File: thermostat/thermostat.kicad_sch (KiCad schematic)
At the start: 14 parts, among them J1 Conn_01x16, J2 Conn_01x12, J3 Conn_01x05, SW1 EVP-AEBB2A, U1 ATSAMD21G18A-A, U2 SPX3819M5-L-3-3, U3 SS-52400-002, Y1 Crystal

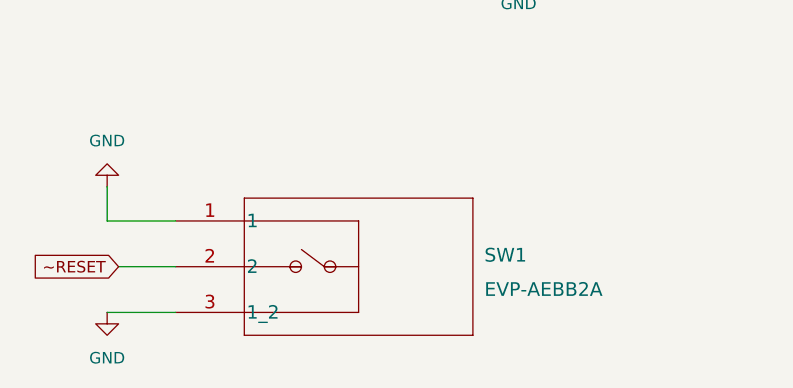
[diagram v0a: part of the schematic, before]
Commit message: thermostat: Use switch
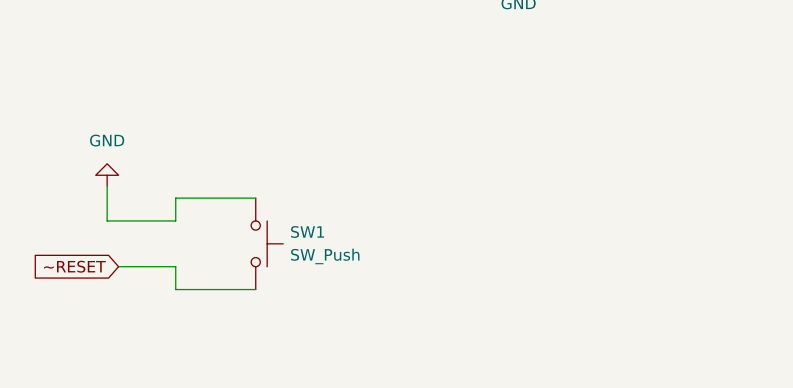
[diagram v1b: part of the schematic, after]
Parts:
- removed SW1: EVP-AEBB2A, SW_EVPAEBB2A_PAN, symbol SWITCH:EVP-AEBB2A
- added SW1: SW_Push, symbol Switch:SW_Push
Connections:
- net GND: now also SW1.1
- net ~RESET: now also SW1.2
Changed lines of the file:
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@@
+    (stroke (width 0) (type default) (color 0 0 0 0))
+  )
+  (wire (pts (xy 52.07 166.37) (xy 60.96 166.37))
     (stroke (width 0) (type default) (color 0 0 0 0))
   )
@@
     (stroke (width 0) (type default) (color 0 0 0 0))
   )
+  (wire (pts (xy 52.07 173.99) (xy 52.07 176.53))
+    (stroke (width 0) (type default) (color 0 0 0 0))
+  )
   (wire (pts (xy 82.55 27.94) (xy 90.17 27.94))
     (stroke (width 0) (type default) (color 0 0 0 0))
@@
     (stroke (width 0) (type default) (color 0 0 0 0))
   )
+  (wire (pts (xy 52.07 168.91) (xy 52.07 166.37))
+    (stroke (width 0) (type default) (color 0 0 0 0))
+  )
   (wire (pts (xy 137.16 146.05) (xy 142.24 146.05))
     (stroke (width 0) (type default) (color 0 0 0 0))
@@
     (stroke (width 0) (type default) (color 0 0 0 0))
   )
-  (wire (pts (xy 44.45 179.07) (xy 52.07 179.07))
-    (stroke (width 0) (type default) (color 0 0 0 0))
-  )
   (wire (pts (xy 214.63 92.71) (xy 215.9 92.71))
     (stroke (width 0) (type default) (color 0 0 0 0))
@@
   )
   (wire (pts (xy 137.16 158.75) (xy 142.24 158.75))
+    (stroke (width 0) (type default) (color 0 0 0 0))
+  )
+  (wire (pts (xy 52.07 176.53) (xy 60.96 176.53))
     (stroke (width 0) (type default) (color 0 0 0 0))
   )
@@
     (pin "1")
   )
+  (symbol (lib_id "Switch:SW_Push") (at 60.96 171.45 270) (unit 1)
+    (in_bom yes) (on_board yes) (fields_autoplaced)
+    (property "Reference" "SW1" (id 0) (at 64.77 170.1799 90)
+      (effects (font (size 1.27 1.27)) (justify left))
+    )
+    (property "Value" "SW_Push" (id 1) (at 64.77 172.7199 90)
+      (effects (font (size 1.27 1.27)) (justify left))
+    )
+    (property "Footprint" "" (id 2) (at 66.04 171.45 0)
+      (effects (font (size 1.27 1.27)) hide)
+    )
+    (property "Datasheet" "~" (id 3) (at 66.04 171.45 0)
+      (effects (font (size 1.27 1.27)) hide)
+    )
+    (pin "1")
+    (pin "2")
+  )
   (symbol (lib_id "Device:R") (at 210.82 92.71 270) (unit 1)
     (in_bom yes) (on_board yes) (fields_autoplaced)
@@
     )
     (pin "1")
-  )
-  (symbol (lib_id "SWITCH:EVP-AEBB2A") (at 52.07 168.91 0) (unit 1)
-    (in_bom yes) (on_board yes) (fields_autoplaced)
-    (property "Reference" "SW1" (id 0) (at 86.36 172.72 0)
-      (effects (font (size 1.524 1.524)) (justify left))
-    )
-    (property "Value" "EVP-AEBB2A" (id 1) (at 86.36 176.53 0)
-      (effects (font (size 1.524 1.524)) (justify left))
-    )
-    (property "Footprint" "SW_EVPAEBB2A_PAN" (id 2) (at 72.39 165.354 0)
-      (effects (font (size 1.524 1.524)) hide)
-    )
-    (property "Datasheet" "" (id 3) (at 52.07 168.91 0)
-      (effects (font (size 1.524 1.524)))
-    )
-    (pin "1")
-    (pin "2")
-    (pin "3")
   )
   (symbol (lib_id "Device:R") (at 266.7 149.86 0) (unit 1)
@@
     (pin "1")
   )
-  (symbol (lib_id "power:GND") (at 44.45 179.07 0) (unit 1)
-    (in_bom yes) (on_board yes) (fields_autoplaced)
-    (property "Reference" "#PWR0116" (id 0) (at 44.45 185.42 0)
-      (effects (font (size 1.27 1.27)) hide)
-    )
-    (property "Value" "GND" (id 1) (at 44.45 184.15 0))
-    (property "Footprint" "" (id 2) (at 44.45 179.07 0)
-      (effects (font (size 1.27 1.27)) hide)
-    )
-    (property "Datasheet" "" (id 3) (at 44.45 179.07 0)
-      (effects (font (size 1.27 1.27)) hide)
-    )
-    (pin "1")
-  )
   (symbol (lib_id "power:GND") (at 142.24 167.64 0) (unit 1)
     (in_bom yes) (on_board yes) (fields_autoplaced)
@@
       (reference "#PWR0115") (unit 1) (value "GND") (footprint "")
     )
-    (path "/b3fbe975-45ea-44a8-87b8-c7050712856c"
-      (reference "#PWR0116") (unit 1) (value "GND") (footprint "")
-    )
     (path "/5399cb33-2c88-49aa-abea-3ab09457e0ba"
       (reference "#PWR0117") (unit 1) (value "GND") (footprint "")
@@
       (reference "R3") (unit 1) (value "100k") (footprint "")
     )
-    (path "/5cb38285-3deb-4540-8ecc-fbfb8f0610f8"
-      (reference "SW1") (unit 1) (value "EVP-AEBB2A") (footprint "SW_EVPAEBB2A_PAN")
+    (path "/4280e647-e2ea-453a-9254-4752d9b95808"
+      (reference "SW1") (unit 1) (value "SW_Push") (footprint "")
     )
     (path "/76387972-e37b-48f4-8f5f-9bf11be0c89f"
